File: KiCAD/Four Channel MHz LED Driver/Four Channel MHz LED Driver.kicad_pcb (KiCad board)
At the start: 2 copper layers, 100 x 100 mm, 92 parts, among them J1 Barrel_Jack_Switch, J10 Conn_01x24_Female, J2 Conn_01x02_Female, J3 8P8C_Shielded_x4, J4 Conn_01x03_Male, J5 Conn_01x03_Female, J6 Conn_01x08_Female, J7 Conn_01x03_Female, J8 Conn_01x05_Female, J9 Conn_01x24_Female, M1 Fan_4pin, Q1 SUM70060E, SW1 Pushbutton_with_LED, SW2 Pushbutton_with_LED, SW3 Pushbutton_with_LED, SW4 Pushbutton_with_LED, SW5 SW_SPDT, U1 12V boost, U10 ASSR-1218, U11 ASSR-1218, U12 Teensy3.6, U2 SN74LV4T125PWR, U3 DPBW06F-05, U4 TMUX1204DGSR, U5 BDJ0GA5WEFJ-E2, U6 ADP7182AUJZ-1.8-R7, U7 LT6200CS8-10, U8 ASSR-1218, U9 ASSR-1218

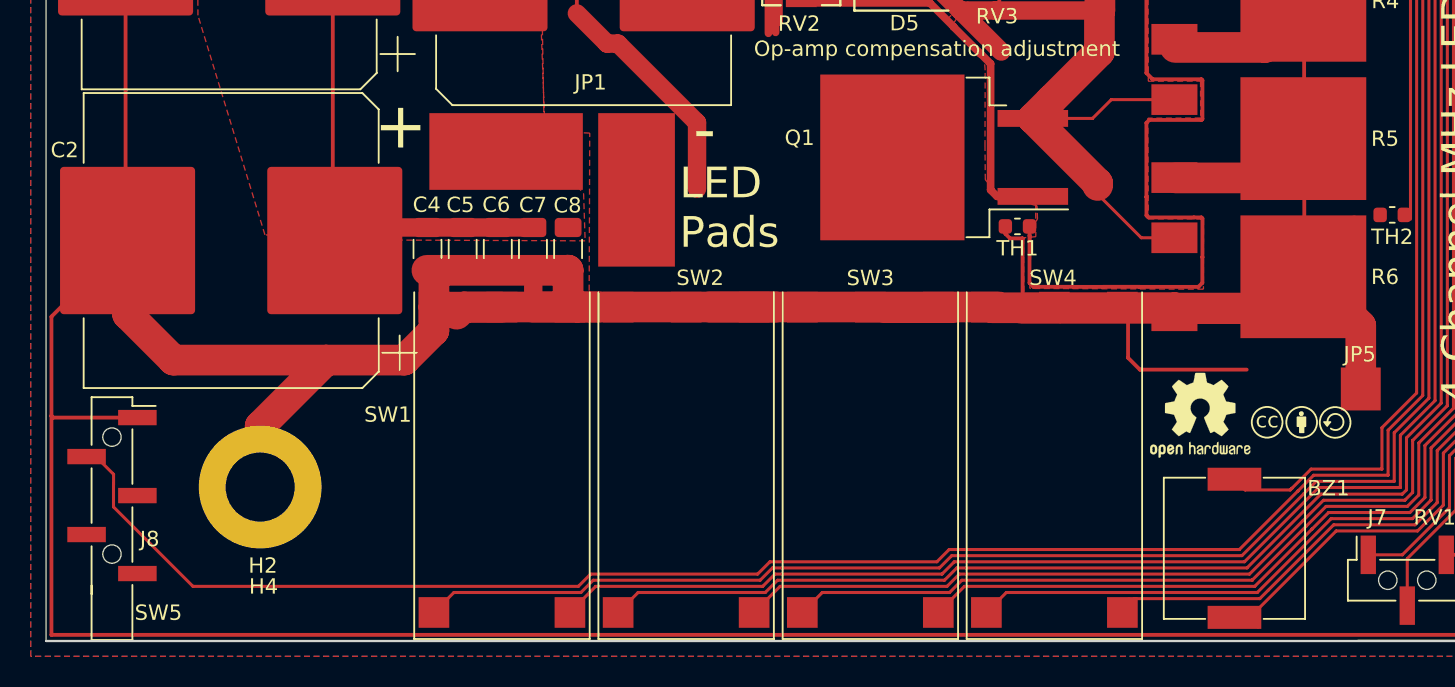
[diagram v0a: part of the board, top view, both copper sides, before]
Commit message: Cap courtyard fixed
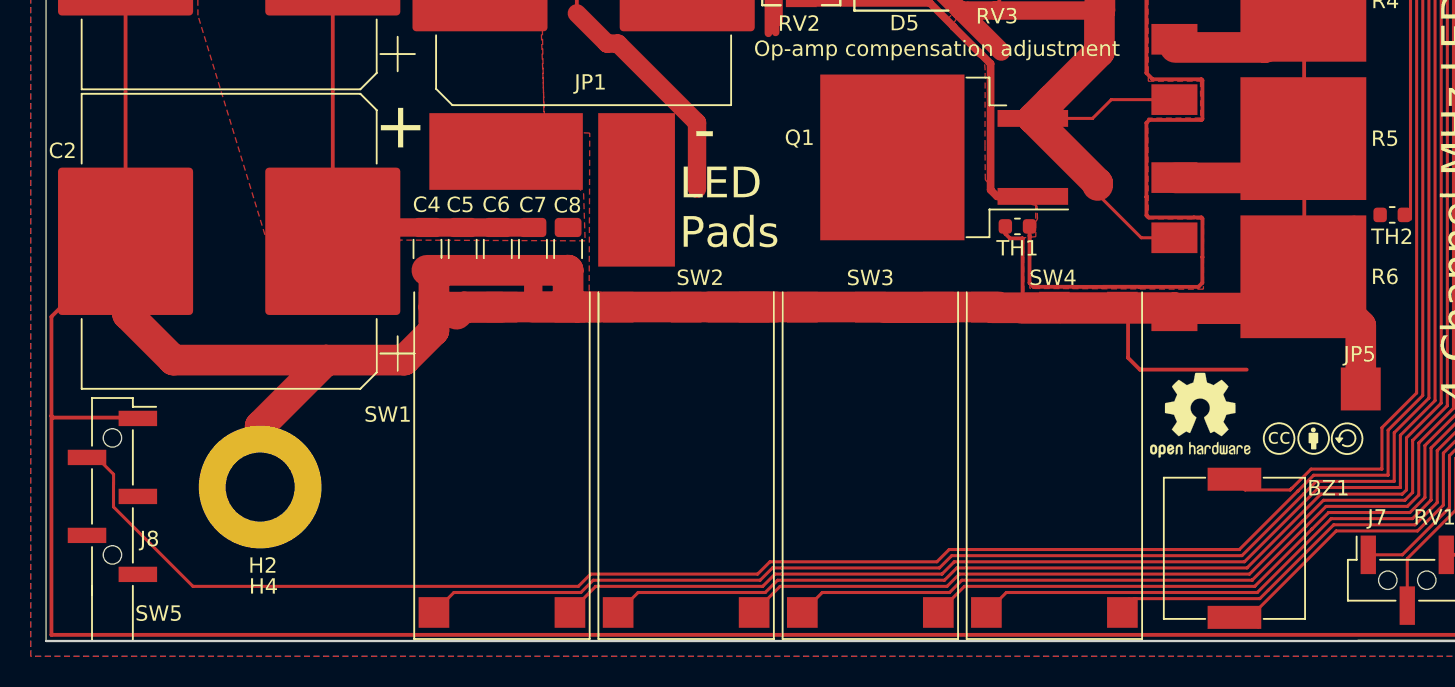
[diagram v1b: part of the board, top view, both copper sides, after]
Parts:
- moved LOGO1 1.32 mm to (118.3, 109.7)
- moved C2 0.14 mm to (48.9, 98.0)
- moved SW5 0.06 mm to (41.3, 114.6)
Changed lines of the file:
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@@
   )
   (module "Custom Footprints:Creative_commons_license" (layer F.Cu)
-    (at 117.55 108.62)
+    (at 118.33 109.68)
     (fp_text reference LOGO1 (at 0.16 -1.67) (layer Dwgs.User) hide
       (effects (font (size 1 1) (thickness 0.15)))
@@
   )
   (module Capacitor_SMD:CP_Elec_18x22 (layer F.Cu)
-    (at 49.06 97.91 180)
+    (at 48.93 97.96 180)
     (descr "SMD capacitor, aluminum electrolytic, Vishay 1821, 18.0x22.0mm, http://www.vishay.com/docs/28395/150crz.pdf")
     (tags "capacitor electrolytic")
@@
   )
   (module "Custom Footprints:1x5_header_SSM-105-L-SV-BE-LC" (layer F.Cu)
-    (at 41.295001 114.525001)
+    (at 41.325 114.58)
     (descr "surface-mounted straight pin header, 1x05, 2.54mm pitch, single row, style 2 (pin 1 right)")
     (tags "Surface mounted pin header SMD 1x05 2.54mm single row style2 pin1 right")

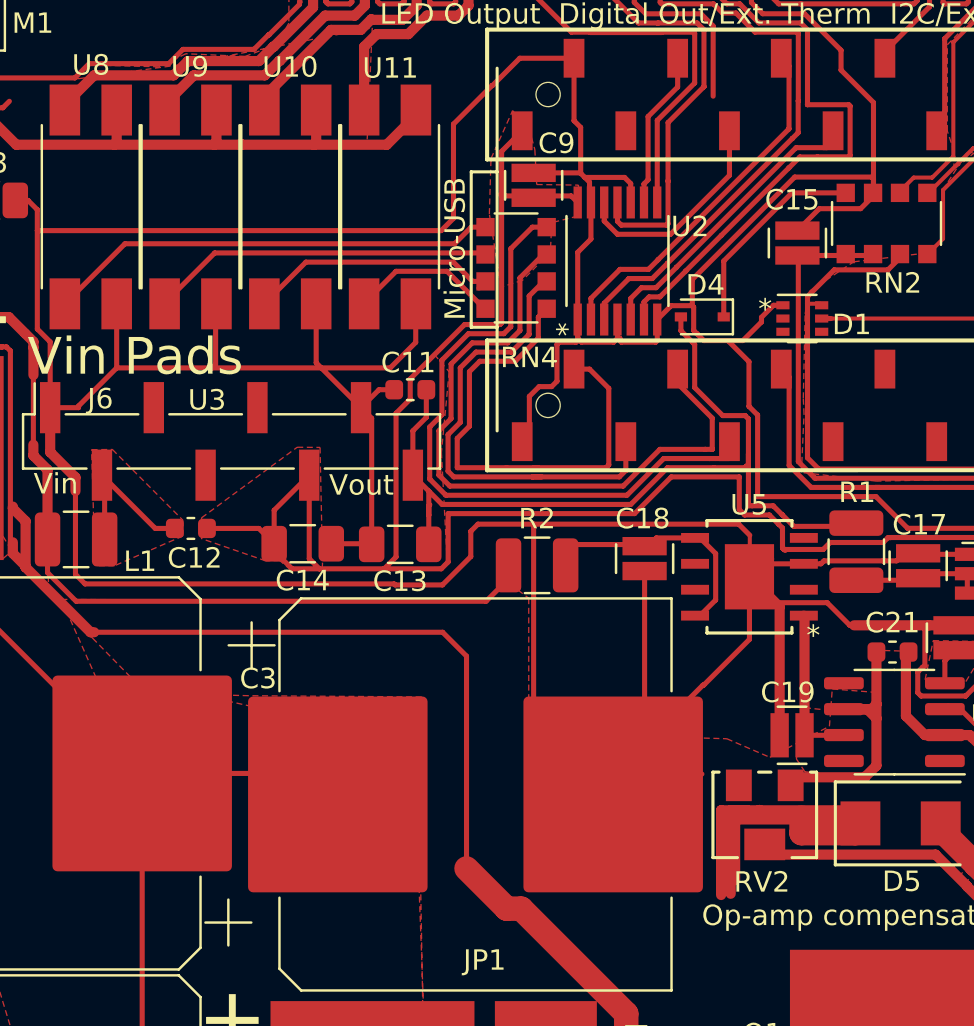
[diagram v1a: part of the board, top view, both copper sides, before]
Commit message: All courtyards fixed except for essential overlaps
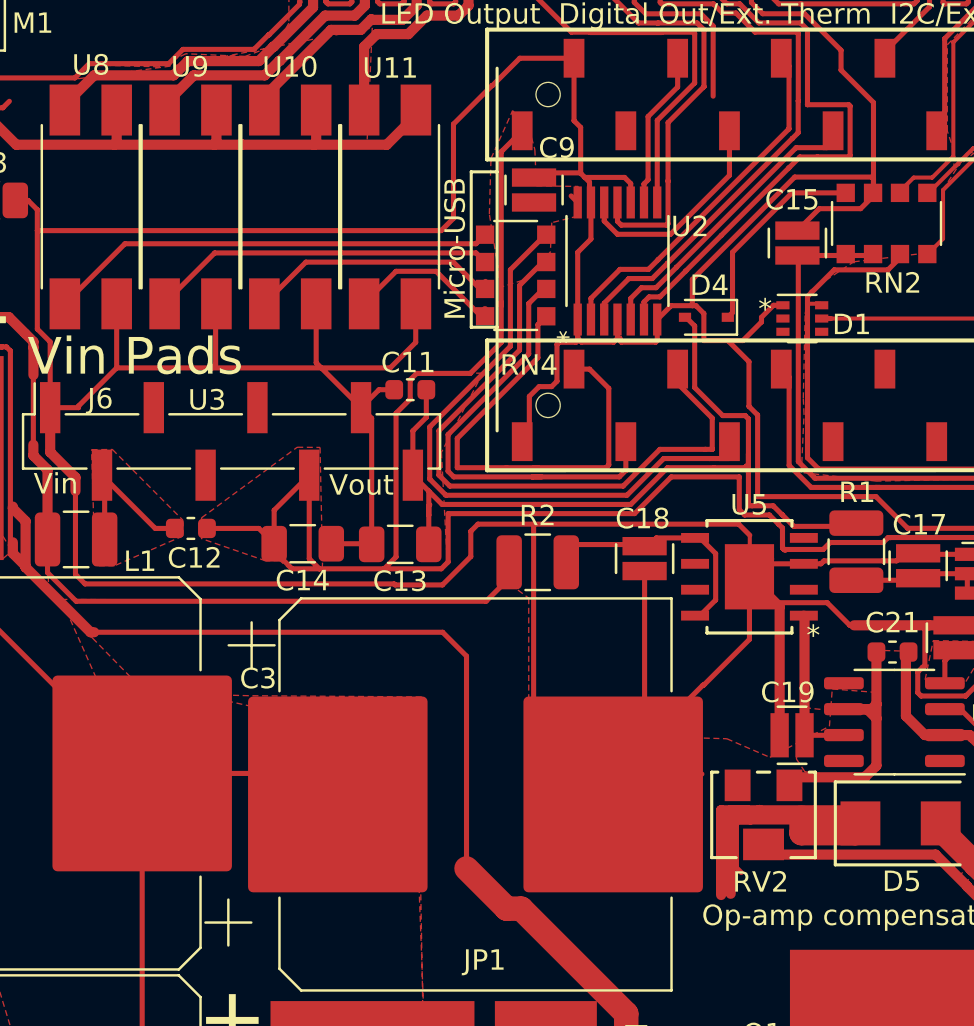
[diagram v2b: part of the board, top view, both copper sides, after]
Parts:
- moved RN4 0.37 mm to (74.0, 54.0)
- moved C9 0.23 mm to (74.9, 49.9)
- moved D4 0.20 mm to (83.3, 56.1)
- moved R2 0.15 mm to (75.1, 68.1)
- moved RV2 0.06 mm to (86.1, 80.5)
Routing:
- net /5V: track 106.4 -> 103.5 mm
- net /Relay4: track 32.8 -> 31.0 mm
- net /Relay3: track 34.1 -> 32.7 mm
- net /Relay1: track 24.2 -> 22.8 mm
- net /Relay2: track 23.2 -> 21.8 mm

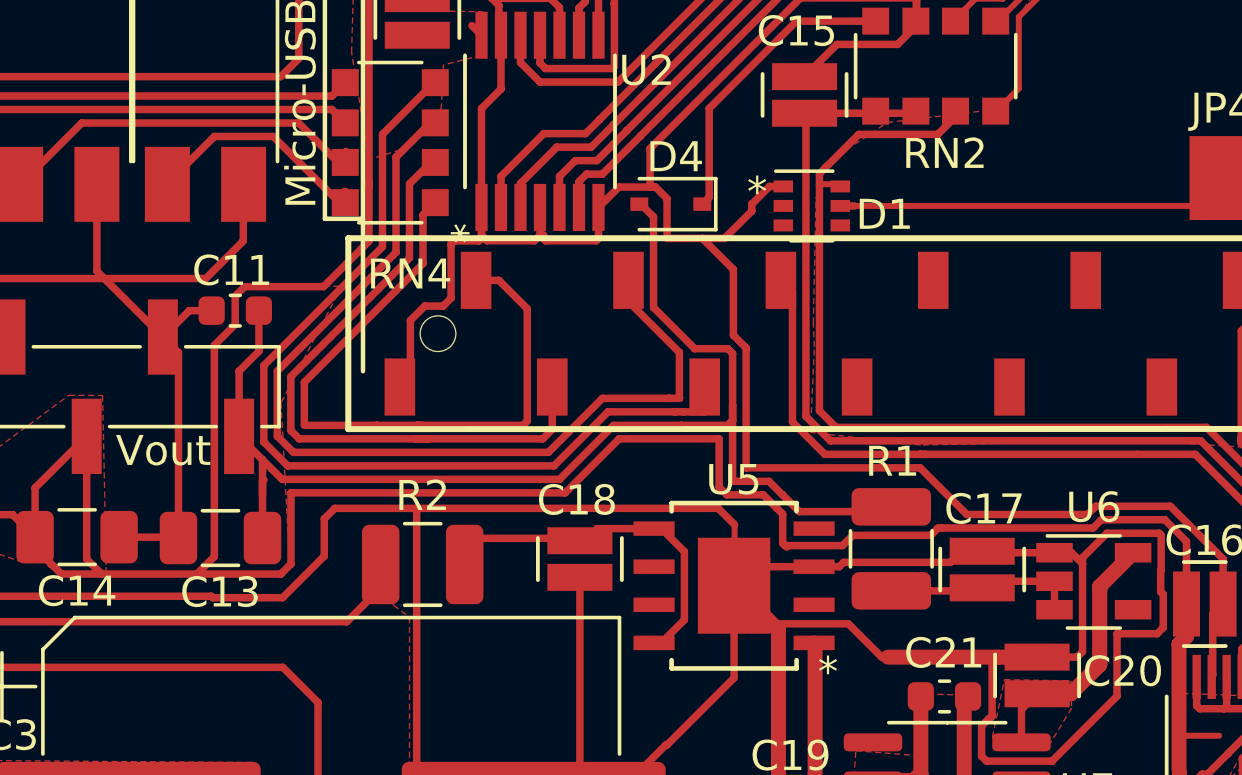
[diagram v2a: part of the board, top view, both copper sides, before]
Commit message: Courtyard fix and track optimization
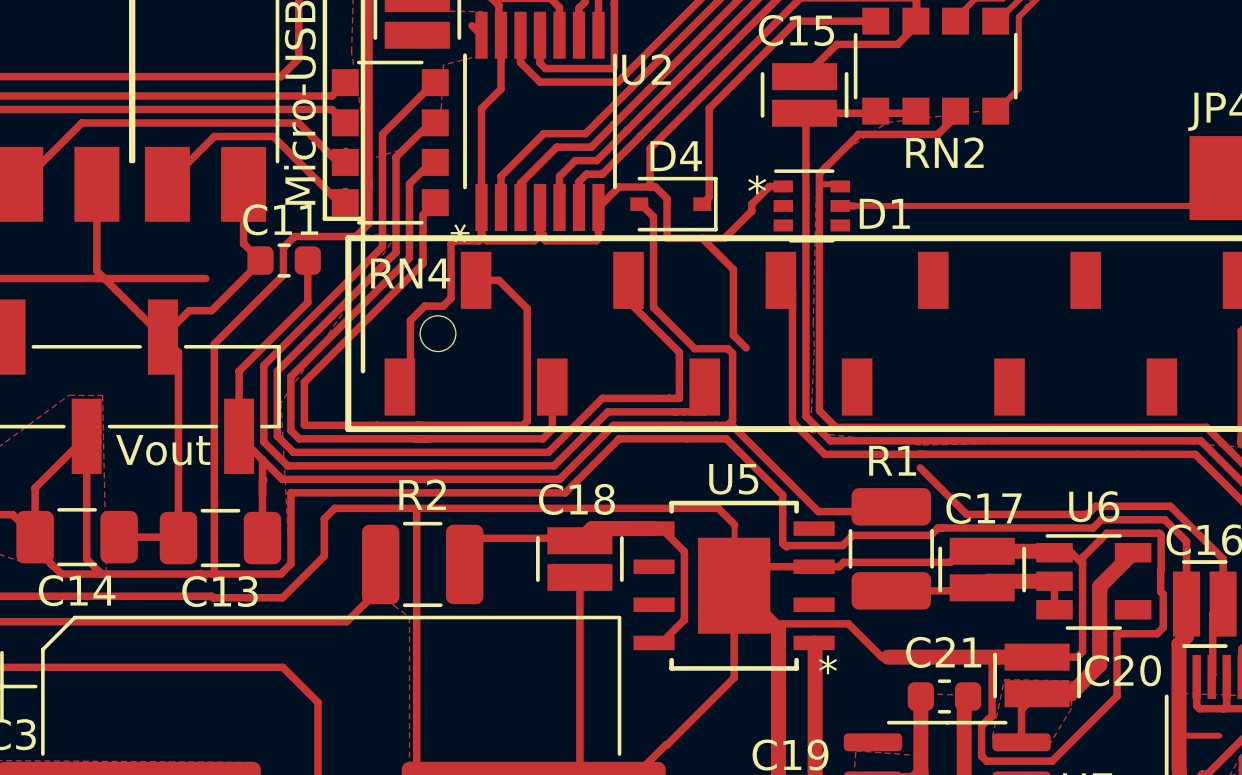
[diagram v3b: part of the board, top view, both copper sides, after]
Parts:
- moved C11 2.33 mm to (70.5, 58.0)
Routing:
- net GND: track 1158.8 -> 1150.5 mm
- net /5V: track 103.5 -> 102.4 mm
- net /-5V: track 43.5 -> 44.2 mm

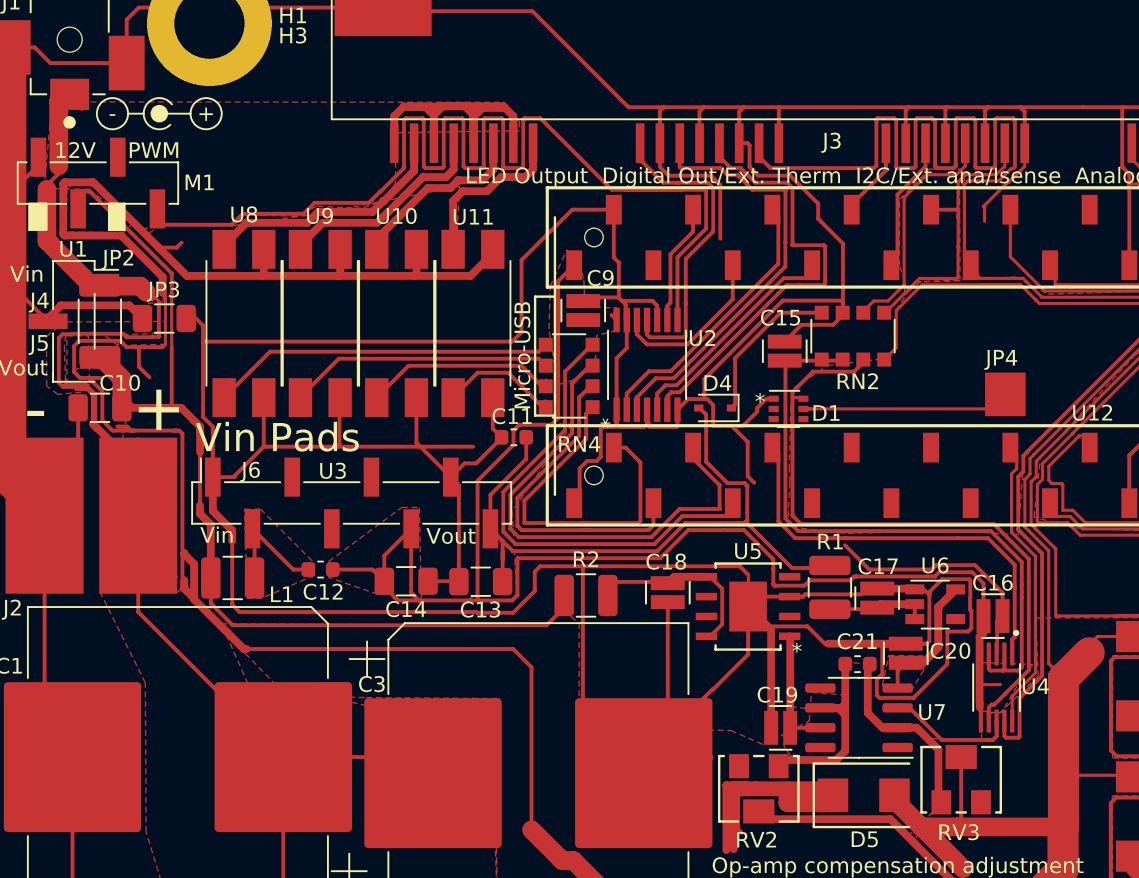
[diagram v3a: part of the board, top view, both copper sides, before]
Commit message: Improved heatsink positioning
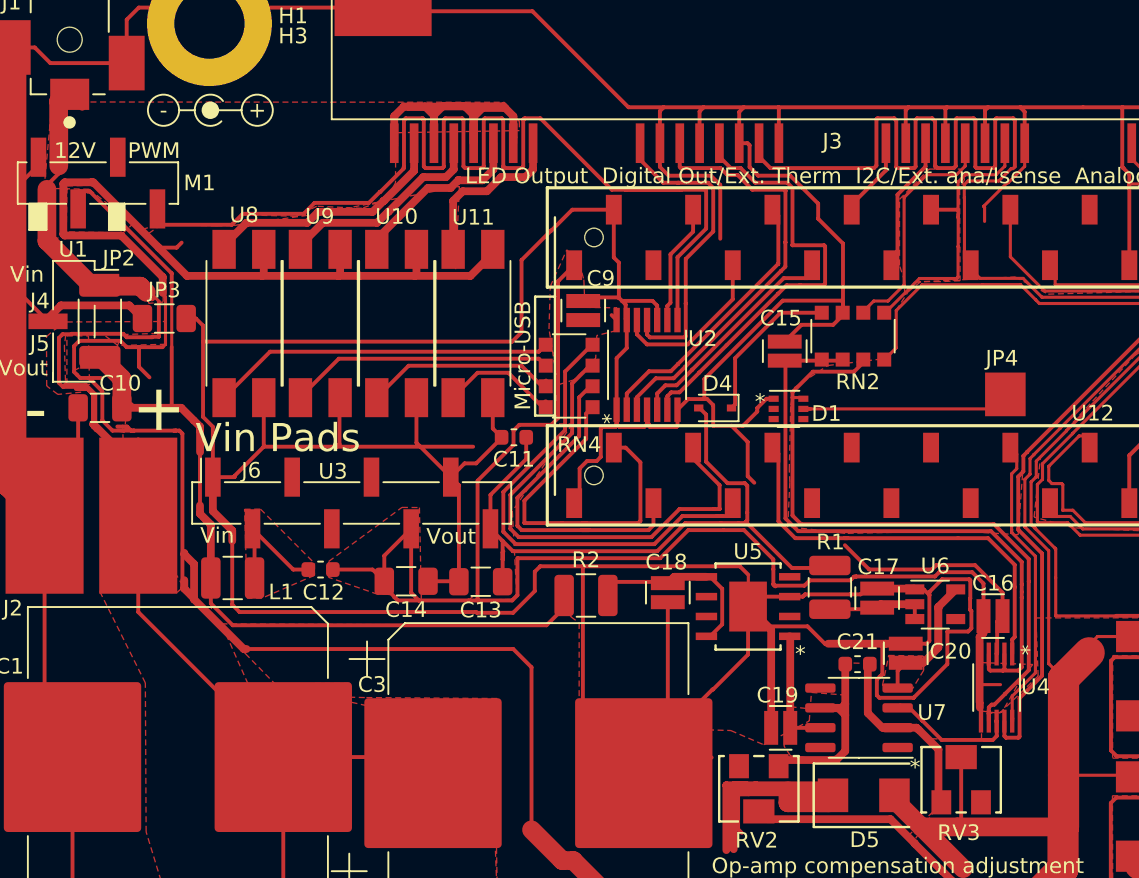
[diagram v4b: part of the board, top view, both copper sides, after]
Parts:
- moved HS3 52.8 mm to (128.6, 28.6)
- moved HS4 40.7 mm to (88.1, 37.9), turned to 180 degrees
- moved HS1 5.11 mm to (95.9, 78.4)
- moved HS2 3.35 mm to (136.4, 69.2)
- moved LOGO2 3.28 mm to (51.0, 31.0)
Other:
- board text added: "*"

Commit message: more HS optimization
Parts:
- moved HS4 1.63 mm to (88.2, 36.3)
- moved HS1 1.59 mm to (95.9, 76.8)
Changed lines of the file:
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@@
   )
   (module "Custom Footprints:Heatsink_910-40-2-23-2-B-0" (layer B.Cu)
-    (at 88.14 37.91 180)
+    (at 88.15 36.28 180)
     (fp_text reference HS4 (at 21.1 1.2) (layer B.SilkS)
       (effects (font (size 1 1) (thickness 0.15)) (justify mirror))
@@
   )
   (module "Custom Footprints:Heatsink_910-40-2-23-2-B-0" (layer B.Cu)
-    (at 95.87 78.4 180)
+    (at 95.92 76.81 180)
     (fp_text reference HS1 (at 21.1 1.2) (layer B.SilkS)
       (effects (font (size 1 1) (thickness 0.15)) (justify mirror))
